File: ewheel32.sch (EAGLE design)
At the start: 202 parts, among them Q1 32.768kHz, Q2 8MHz, U1 MK22DX256VLF5, U10 MC74HC595ADTR2G, U11 MC74HC595ADTR2G, U12 MC74HC595ADTR2G, U13 MC74HC595ADTR2G, U14 MC74HC595ADTR2G, U15 MC74HC595ADTR2G, U16 MC74HC595ADTR2G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

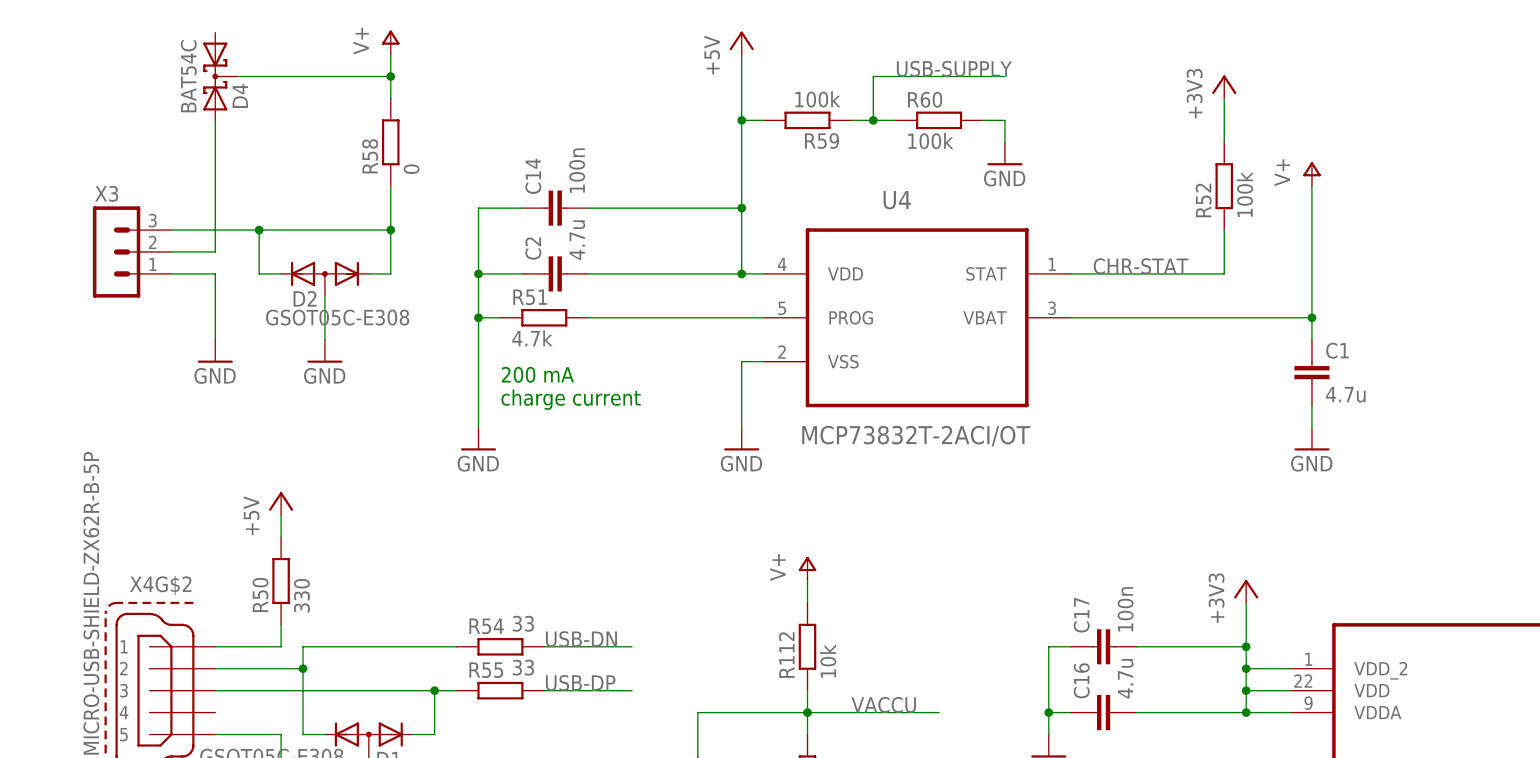
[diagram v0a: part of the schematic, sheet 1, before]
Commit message: Schottky diode for charger
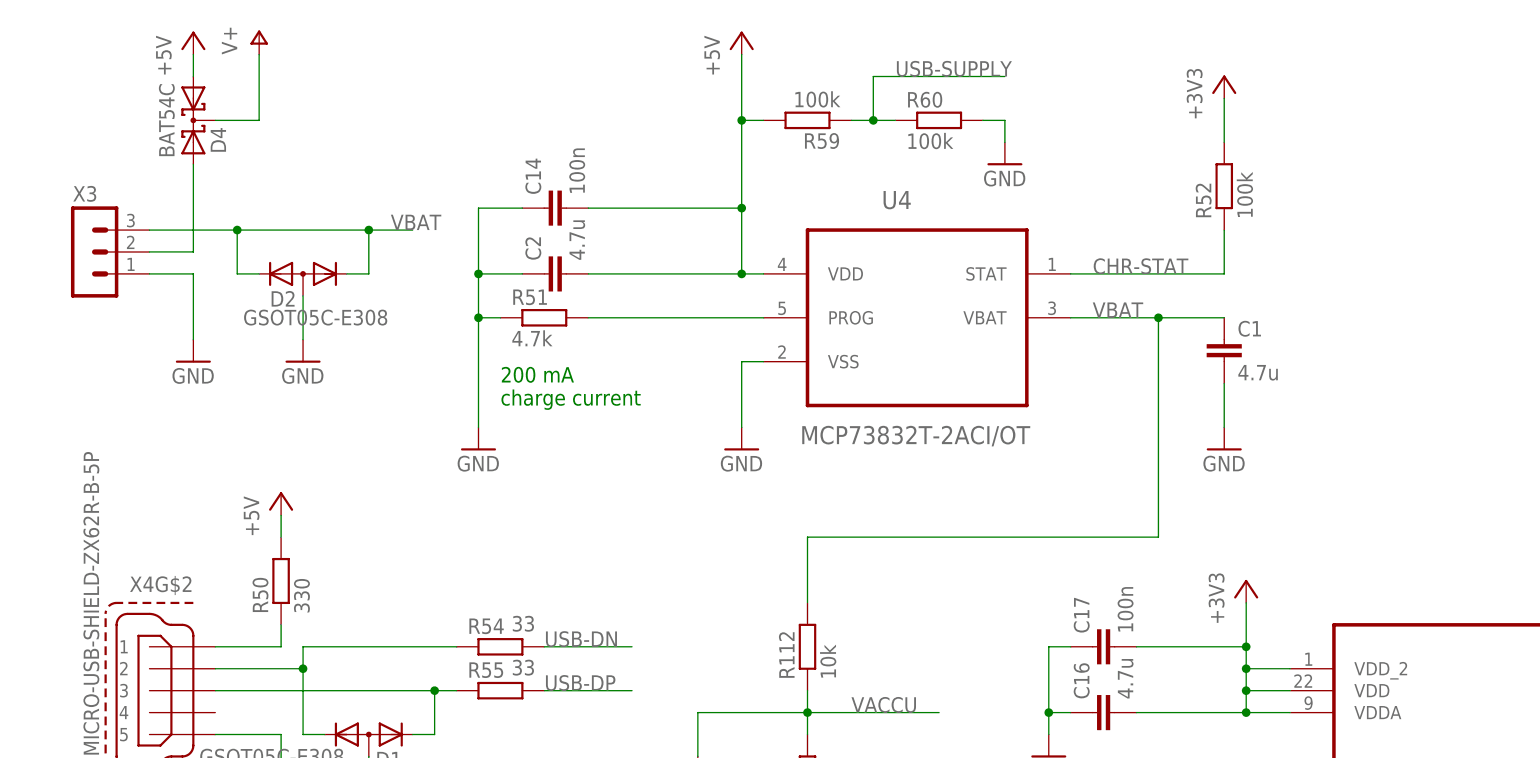
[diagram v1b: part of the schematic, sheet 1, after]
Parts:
- removed R58: 0, resistor:R-EU_R1206
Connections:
- removed net N$54: D2.K1, D2.K2, R58.1, X3.3
- new net VBAT: C1.1, D2.K1, D2.K2, R112.2, U4.VBAT, X3.3
- net +5V: now also D4.A1
- net V+: no longer C1.1, R112.2, R58.2, U4.VBAT
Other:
- moved on the sheet: C1, D2, D4, X3
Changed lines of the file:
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@@
 <?xml version="1.0" encoding="utf-8"?>
 <!DOCTYPE eagle SYSTEM "eagle.dtd">
-<eagle version="6.5.0">
+<eagle version="7.4.0">
 <drawing>
 <settings>
@@
 <part name="X3" library="con-lstb" deviceset="MA03-1" device=""/>
 <part name="P+1" library="supply1" deviceset="V+" device=""/>
-<part name="P+2" library="supply1" deviceset="V+" device=""/>
 <part name="P+3" library="supply1" deviceset="V+" device=""/>
 <part name="GND2" library="supply1" deviceset="GND" device=""/>
@@
 <part name="GND27" library="supply1" deviceset="GND" device=""/>
 <part name="D2" library="diode" deviceset="DIODE-2CA|AC" device="SOT23" value="GSOT05C-E308"/>
-<part name="R58" library="resistor" deviceset="R-EU_" device="R1206" value="0"/>
 <part name="GND28" library="supply1" deviceset="GND" device=""/>
 <part name="C16" library="resistor" deviceset="C-EU" device="C1206" value="4.7u"/>
@@
 <part name="R112" library="resistor" deviceset="R-EU_" device="R0805" value="10k"/>
 <part name="R113" library="resistor" deviceset="R-EU_" device="R0805" value="2.2k"/>
-<part name="P+4" library="supply1" deviceset="V+" device=""/>
 <part name="C20" library="resistor" deviceset="C-EU" device="C0805" value="100n"/>
 <part name="C22" library="resistor" deviceset="C-EU" device="C1206" value="4.7u"/>
@@
 <part name="R60" library="resistor" deviceset="R-EU_" device="R0805" value="100k"/>
 <part name="GND55" library="supply1" deviceset="GND" device=""/>
+<part name="P+6" library="supply1" deviceset="+5V" device=""/>
 </parts>
 <sheets>
@@
 <attribute name="VALUE" x="342.9" y="185.42" size="2.1844" layer="96"/>
 </instance>
-<instance part="X3" gate="G$1" x="20.32" y="226.06"/>
-<instance part="P+1" gate="1" x="53.34" y="251.46"/>
-<instance part="P+2" gate="1" x="160.02" y="236.22"/>
+<instance part="X3" gate="G$1" x="17.78" y="226.06"/>
+<instance part="P+1" gate="1" x="38.1" y="251.46"/>
 <instance part="P+3" gate="1" x="203.2" y="233.68"/>
-<instance part="GND2" gate="1" x="33.02" y="213.36"/>
+<instance part="GND2" gate="1" x="30.48" y="213.36"/>
 <instance part="GND4" gate="1" x="93.98" y="203.2"/>
 <instance part="GND6" gate="1" x="144.78" y="35.56"/>
@@
 <instance part="R52" gate="G$1" x="149.86" y="233.68" rot="R90"/>
 <instance part="P+7" gate="1" x="93.98" y="251.46"/>
-<instance part="C1" gate="G$1" x="160.02" y="213.36"/>
+<instance part="C1" gate="G$1" x="149.86" y="215.9"/>
 <instance part="C2" gate="G$1" x="71.12" y="223.52" rot="R90"/>
-<instance part="GND11" gate="1" x="160.02" y="203.2"/>
+<instance part="GND11" gate="1" x="149.86" y="203.2"/>
 <instance part="R53" gate="G$1" x="76.2" y="43.18" rot="R90"/>
 <instance part="R49" gate="G$1" x="20.32" y="50.8" rot="R90"/>
@@
 <instance part="C15" gate="G$1" x="195.58" y="213.36"/>
 <instance part="GND27" gate="1" x="195.58" y="203.2"/>
-<instance part="D2" gate="G$1" x="45.72" y="223.52" smashed="yes" rot="R180">
-<attribute name="NAME" x="44.958" y="221.5134" size="1.778" layer="95" rot="R180"/>
-<attribute name="VALUE" x="55.626" y="219.3544" size="1.778" layer="96" rot="R180"/>
+<instance part="D2" gate="G$1" x="43.18" y="223.52" smashed="yes" rot="R180">
+<attribute name="NAME" x="42.418" y="221.5134" size="1.778" layer="95" rot="R180"/>
+<attribute name="VALUE" x="53.086" y="219.3544" size="1.778" layer="96" rot="R180"/>
 </instance>
-<instance part="R58" gate="G$1" x="53.34" y="238.76" rot="R90"/>
-<instance part="GND28" gate="1" x="45.72" y="213.36"/>
+<instance part="GND28" gate="1" x="43.18" y="213.36"/>
 <instance part="C16" gate="G$1" x="134.62" y="172.72" rot="R90"/>
 <instance part="C17" gate="G$1" x="134.62" y="180.34" rot="R90"/>
@@
 <instance part="R112" gate="G$1" x="101.6" y="180.34" rot="R90"/>
 <instance part="R113" gate="G$1" x="101.6" y="165.1" rot="R90"/>
-<instance part="P+4" gate="1" x="101.6" y="190.5"/>
 <instance part="C20" gate="G$1" x="88.9" y="165.1"/>
 <instance part="C22" gate="G$1" x="43.18" y="142.24"/>
@@
 <instance part="GND49" gate="1" x="48.26" y="88.9"/>
 <instance part="D3" gate="G$1" x="43.18" y="111.76" rot="R270"/>
-<instance part="D4" gate="G$1" x="33.02" y="246.38" rot="R270"/>
+<instance part="D4" gate="G$1" x="30.48" y="241.3" rot="R270"/>
 <instance part="C24" gate="G$1" x="55.88" y="142.24"/>
 <instance part="GND50" gate="1" x="55.88" y="132.08"/>
@@
 <instance part="R60" gate="G$1" x="116.84" y="241.3"/>
 <instance part="GND55" gate="1" x="124.46" y="236.22"/>
+<instance part="P+6" gate="1" x="30.48" y="251.46"/>
 </instances>
 <busses>
@@
 <segment>
 <pinref part="X3" gate="G$1" pin="1"/>
-<wire x1="27.94" y1="223.52" x2="33.02" y2="223.52" width="0.1524" layer="91"/>
-<wire x1="33.02" y1="223.52" x2="33.02" y2="215.9" width="0.1524" layer="91"/>
+<wire x1="25.4" y1="223.52" x2="30.48" y2="223.52" width="0.1524" layer="91"/>
+<wire x1="30.48" y1="223.52" x2="30.48" y2="215.9" width="0.1524" layer="91"/>
 <pinref part="GND2" gate="1" pin="GND"/>
 </segment>
@@
 <pinref part="C1" gate="G$1" pin="2"/>
 <pinref part="GND11" gate="1" pin="GND"/>
-<wire x1="160.02" y1="208.28" x2="160.02" y2="205.74" width="0.1524" layer="91"/>
+<wire x1="149.86" y1="210.82" x2="149.86" y2="205.74" width="0.1524" layer="91"/>
 </segment>
 <segment>
@@
 <pinref part="D2" gate="G$1" pin="A"/>
 <pinref part="GND28" gate="1" pin="GND"/>
-<wire x1="45.72" y1="220.98" x2="45.72" y2="215.9" width="0.1524" layer="91"/>
+<wire x1="43.18" y1="220.98" x2="43.18" y2="215.9" width="0.1524" layer="91"/>
 </segment>
 <segment>
@@
 </segment>
 <segment>
-<pinref part="U4" gate="A" pin="VBAT"/>
-<pinref part="P+2" gate="1" pin="V+"/>
-<wire x1="132.08" y1="218.44" x2="160.02" y2="218.44" width="0.1524" layer="91"/>
-<wire x1="160.02" y1="218.44" x2="160.02" y2="233.68" width="0.1524" layer="91"/>
-<pinref part="C1" gate="G$1" pin="1"/>
-<wire x1="160.02" y1="218.44" x2="160.02" y2="215.9" width="0.1524" layer="91"/>
-<junction x="160.02" y="218.44"/>
-</segment>
-<segment>
 <pinref part="P+1" gate="1" pin="V+"/>
-<pinref part="R58" gate="G$1" pin="2"/>
-<wire x1="53.34" y1="248.92" x2="53.34" y2="246.38" width="0.1524" layer="91"/>
+<wire x1="38.1" y1="248.92" x2="38.1" y2="241.3" width="0.1524" layer="91"/>
 <pinref part="D4" gate="G$1" pin="CC"/>
-<wire x1="53.34" y1="246.38" x2="53.34" y2="243.84" width="0.1524" layer="91"/>
-<wire x1="35.56" y1="246.38" x2="53.34" y2="246.38" width="0.1524" layer="91"/>
-<junction x="53.34" y="246.38"/>
-</segment>
-<segment>
-<pinref part="R112" gate="G$1" pin="2"/>
-<wire x1="101.6" y1="185.42" x2="101.6" y2="187.96" width="0.1524" layer="91"/>
-<pinref part="P+4" gate="1" pin="V+"/>
+<wire x1="33.02" y1="241.3" x2="38.1" y2="241.3" width="0.1524" layer="91"/>
 </segment>
 <segment>
@@
 <wire x1="40.64" y1="195.58" x2="40.64" y2="193.04" width="0.1524" layer="91"/>
 </segment>
+<segment>
+<pinref part="D4" gate="G$1" pin="A1"/>
+<pinref part="P+6" gate="1" pin="+5V"/>
+<wire x1="30.48" y1="246.38" x2="30.48" y2="248.92" width="0.1524" layer="91"/>
+</segment>
 </net>
 <net name="I2C-SDA" class="0">
@@
 </segment>
 </net>
-<net name="N$54" class="0">
+<net name="VBAT" class="0">
 <segment>
 <pinref part="X3" gate="G$1" pin="3"/>
 <pinref part="D2" gate="G$1" pin="K2"/>
-<wire x1="40.64" y1="223.52" x2="38.1" y2="223.52" width="0.1524" layer="91"/>
-<wire x1="38.1" y1="223.52" x2="38.1" y2="228.6" width="0.1524" layer="91"/>
-<wire x1="38.1" y1="228.6" x2="27.94" y2="228.6" width="0.1524" layer="91"/>
+<wire x1="38.1" y1="223.52" x2="35.56" y2="223.52" width="0.1524" layer="91"/>
+<wire x1="35.56" y1="223.52" x2="35.56" y2="228.6" width="0.1524" layer="91"/>
+<wire x1="35.56" y1="228.6" x2="25.4" y2="228.6" width="0.1524" layer="91"/>
 <pinref part="D2" gate="G$1" pin="K1"/>
-<wire x1="50.8" y1="223.52" x2="53.34" y2="223.52" width="0.1524" layer="91"/>
-<wire x1="53.34" y1="223.52" x2="53.34" y2="228.6" width="0.1524" layer="91"/>
-<wire x1="53.34" y1="228.6" x2="38.1" y2="228.6" width="0.1524" layer="91"/>
-<junction x="38.1" y="228.6"/>
-<pinref part="R58" gate="G$1" pin="1"/>
-<wire x1="53.34" y1="233.68" x2="53.34" y2="228.6" width="0.1524" layer="91"/>
-<junction x="53.34" y="228.6"/>
+<wire x1="48.26" y1="223.52" x2="50.8" y2="223.52" width="0.1524" layer="91"/>
+<wire x1="50.8" y1="223.52" x2="50.8" y2="228.6" width="0.1524" layer="91"/>
+<wire x1="50.8" y1="228.6" x2="35.56" y2="228.6" width="0.1524" layer="91"/>
+<junction x="35.56" y="228.6"/>
+<wire x1="55.88" y1="228.6" x2="50.8" y2="228.6" width="0.1524" layer="91"/>
+<junction x="50.8" y="228.6"/>
+<label x="53.34" y="228.6" size="1.778" layer="95"/>
+</segment>
+<segment>
+<pinref part="U4" gate="A" pin="VBAT"/>
+<wire x1="132.08" y1="218.44" x2="142.24" y2="218.44" width="0.1524" layer="91"/>
+<pinref part="C1" gate="G$1" pin="1"/>
+<label x="134.62" y="218.44" size="1.778" layer="95"/>
+<pinref part="R112" gate="G$1" pin="2"/>
+<wire x1="142.24" y1="218.44" x2="149.86" y2="218.44" width="0.1524" layer="91"/>
+<wire x1="101.6" y1="185.42" x2="101.6" y2="193.04" width="0.1524" layer="91"/>
+<wire x1="101.6" y1="193.04" x2="142.24" y2="193.04" width="0.1524" layer="91"/>
+<wire x1="142.24" y1="193.04" x2="142.24" y2="218.44" width="0.1524" layer="91"/>
+<junction x="142.24" y="218.44"/>
 </segment>
 </net>
@@
 <segment>
 <pinref part="D4" gate="G$1" pin="A2"/>
-<wire x1="33.02" y1="241.3" x2="33.02" y2="226.06" width="0.1524" layer="91"/>
+<wire x1="30.48" y1="236.22" x2="30.48" y2="226.06" width="0.1524" layer="91"/>
 <pinref part="X3" gate="G$1" pin="2"/>
-<wire x1="33.02" y1="226.06" x2="27.94" y2="226.06" width="0.1524" layer="91"/>
-</segment>
-</net>
+<wire x1="30.48" y1="226.06" x2="25.4" y2="226.06" width="0.1524" layer="91"/>
+</segment>
+</net>

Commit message: Intermediate version. Do not use.
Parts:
- removed R50, R63: 330, resistor:R-EU_R1206
- added L1, L2: 3A/0.06OHM, ewheel32:L-EU
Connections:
- removed net N$6: D4.A2, X3.2
- new net SPI-OLED-A0: U1.PTD7
- new net SPI-OLED-CS: U1.PTC7
- net +5V: now also L1.2; no longer R50.2
- net GND: now also L2.2; no longer R63.1
- net N$55: now also L2.1; no longer R63.2
- net N$60: now also L1.1; no longer R50.1
- net V+: now also X3.2
- net VBAT: now also D4.A2
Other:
- note added: "Revision 1.5"
- note removed: "Revision 1.2"
- moved on the sheet: C22, C24, D4

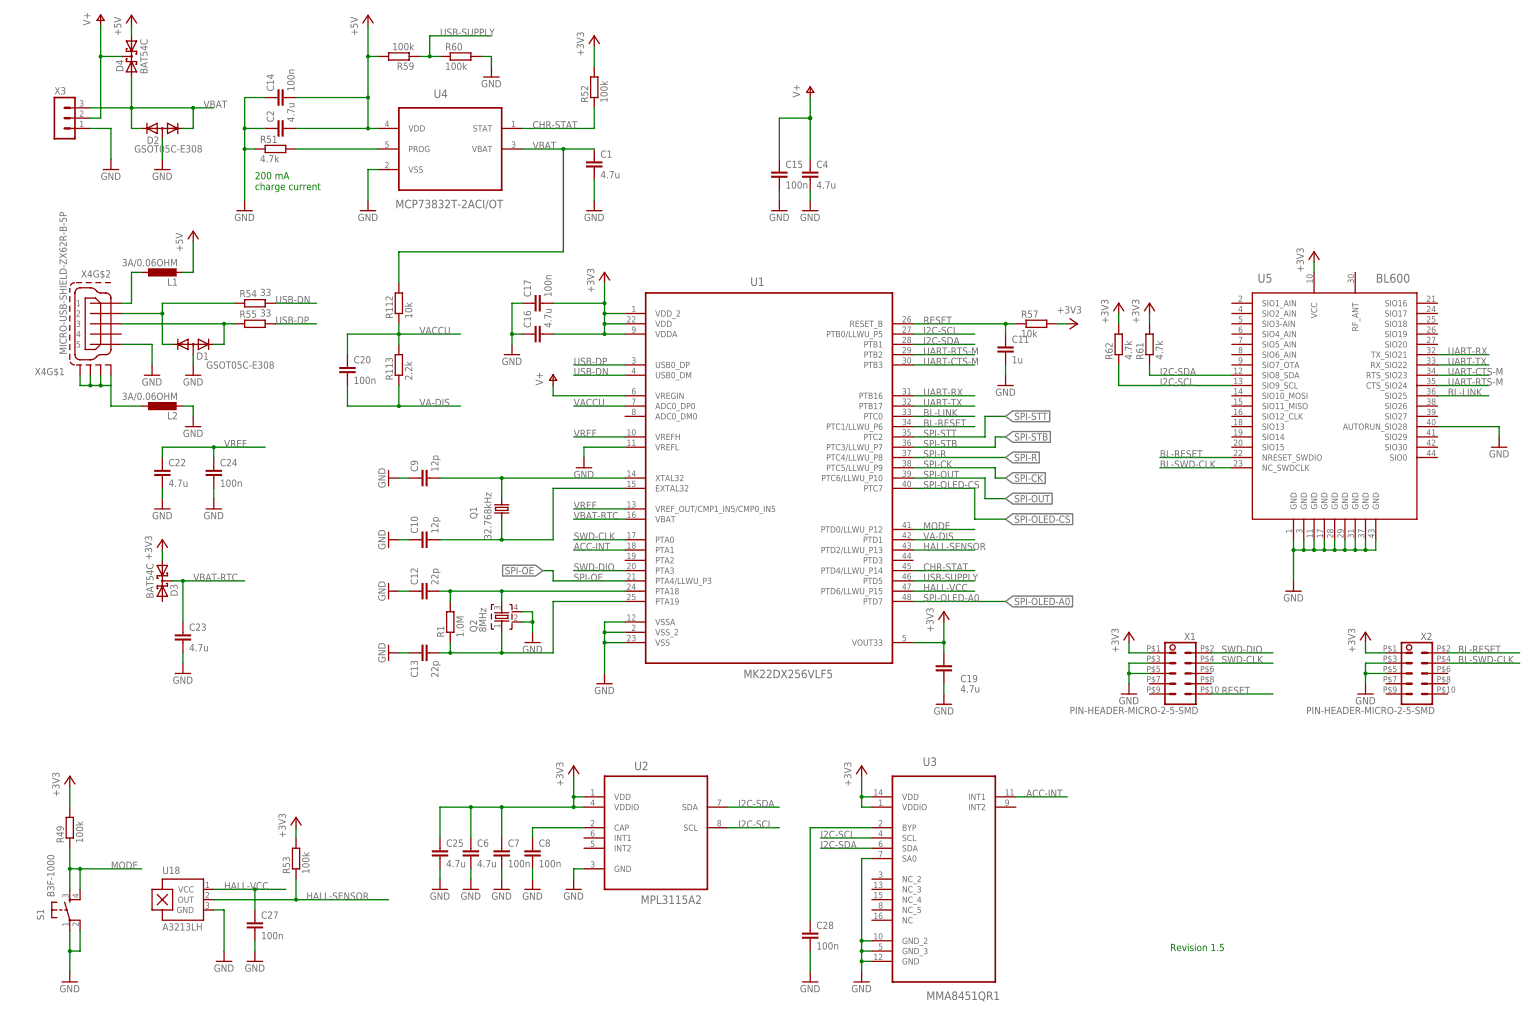
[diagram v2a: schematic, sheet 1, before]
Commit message: Version 1.4. BAT/VCC connector wrong.
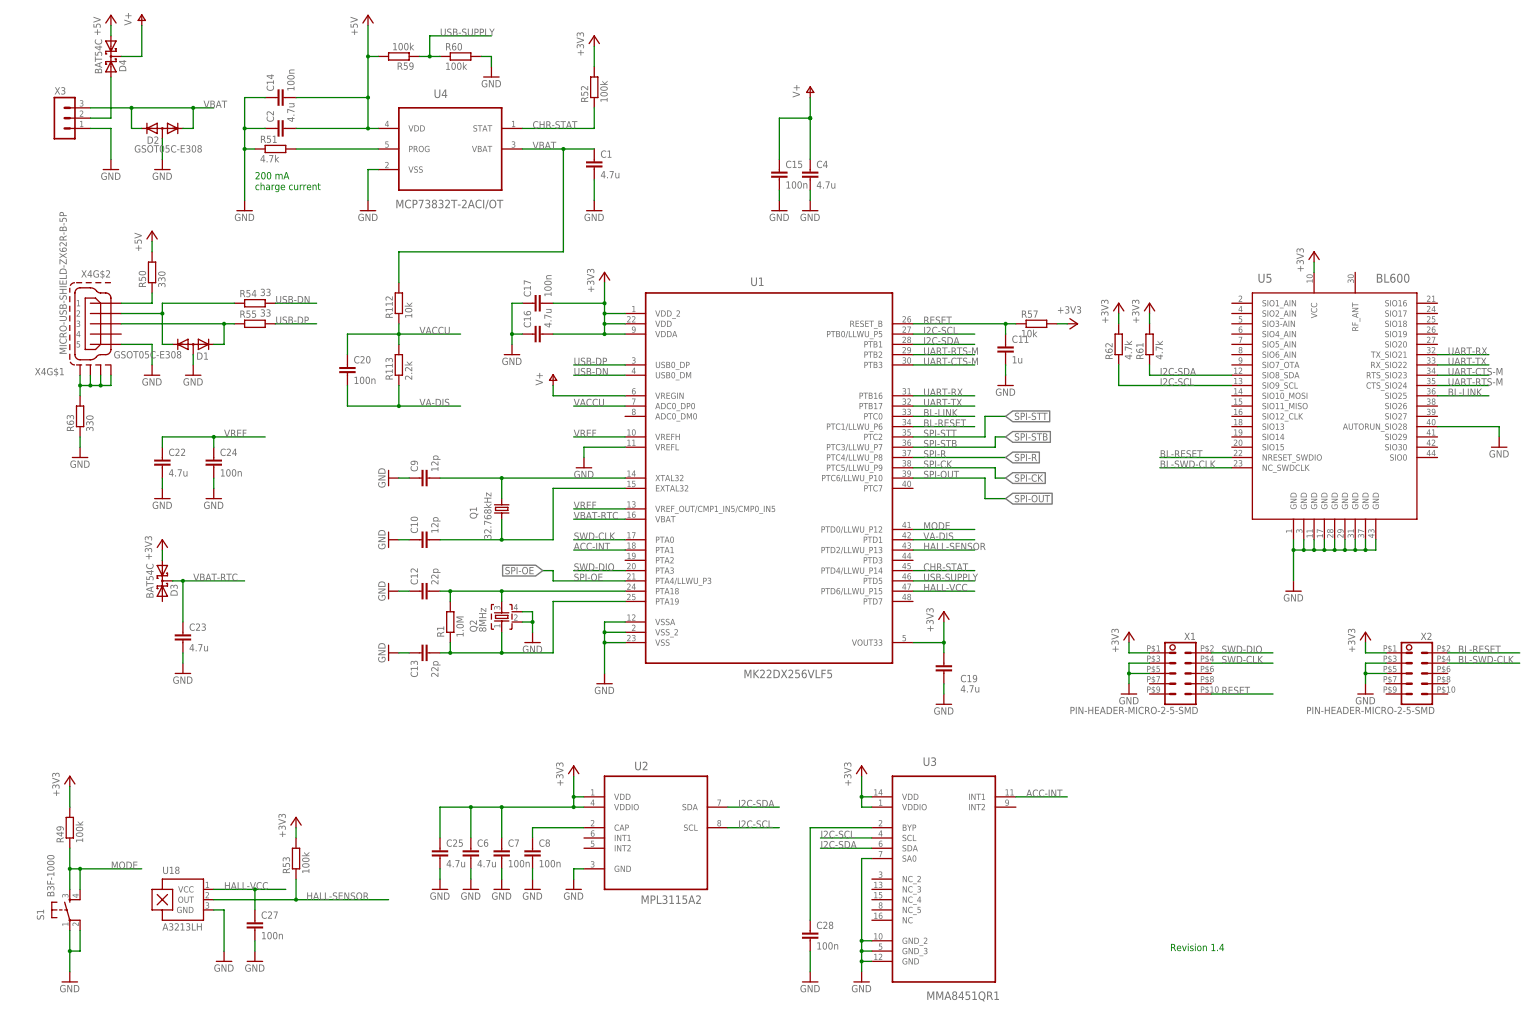
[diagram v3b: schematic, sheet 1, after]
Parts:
- removed L1, L2: 3A/0.06OHM, ewheel32:L-EU
- added R50, R63: 330, resistor:R-EU_R1206
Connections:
- removed net SPI-OLED-A0: U1.PTD7
- removed net SPI-OLED-CS: U1.PTC7
- new net N$6: D4.A2, X3.2
- net +5V: now also R50.2; no longer L1.2
- net GND: now also R63.1; no longer L2.2
- net N$55: now also R63.2; no longer L2.1
- net N$60: now also R50.1; no longer L1.1
- net V+: no longer X3.2
- net VBAT: no longer D4.A2
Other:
- note added: "Revision 1.4"
- note removed: "Revision 1.5"
- moved on the sheet: C22, C24, D4
